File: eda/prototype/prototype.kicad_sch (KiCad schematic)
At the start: 45 parts, among them J1 Conn_02x05_Odd_Even, SW1 SW_DIP_x04, U1 8088_Min_Mode, U10 8255A, U11 8253, U12 8259A, U13 8251, U2 GAL16V8, U3 74HC161, U4 74HC574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

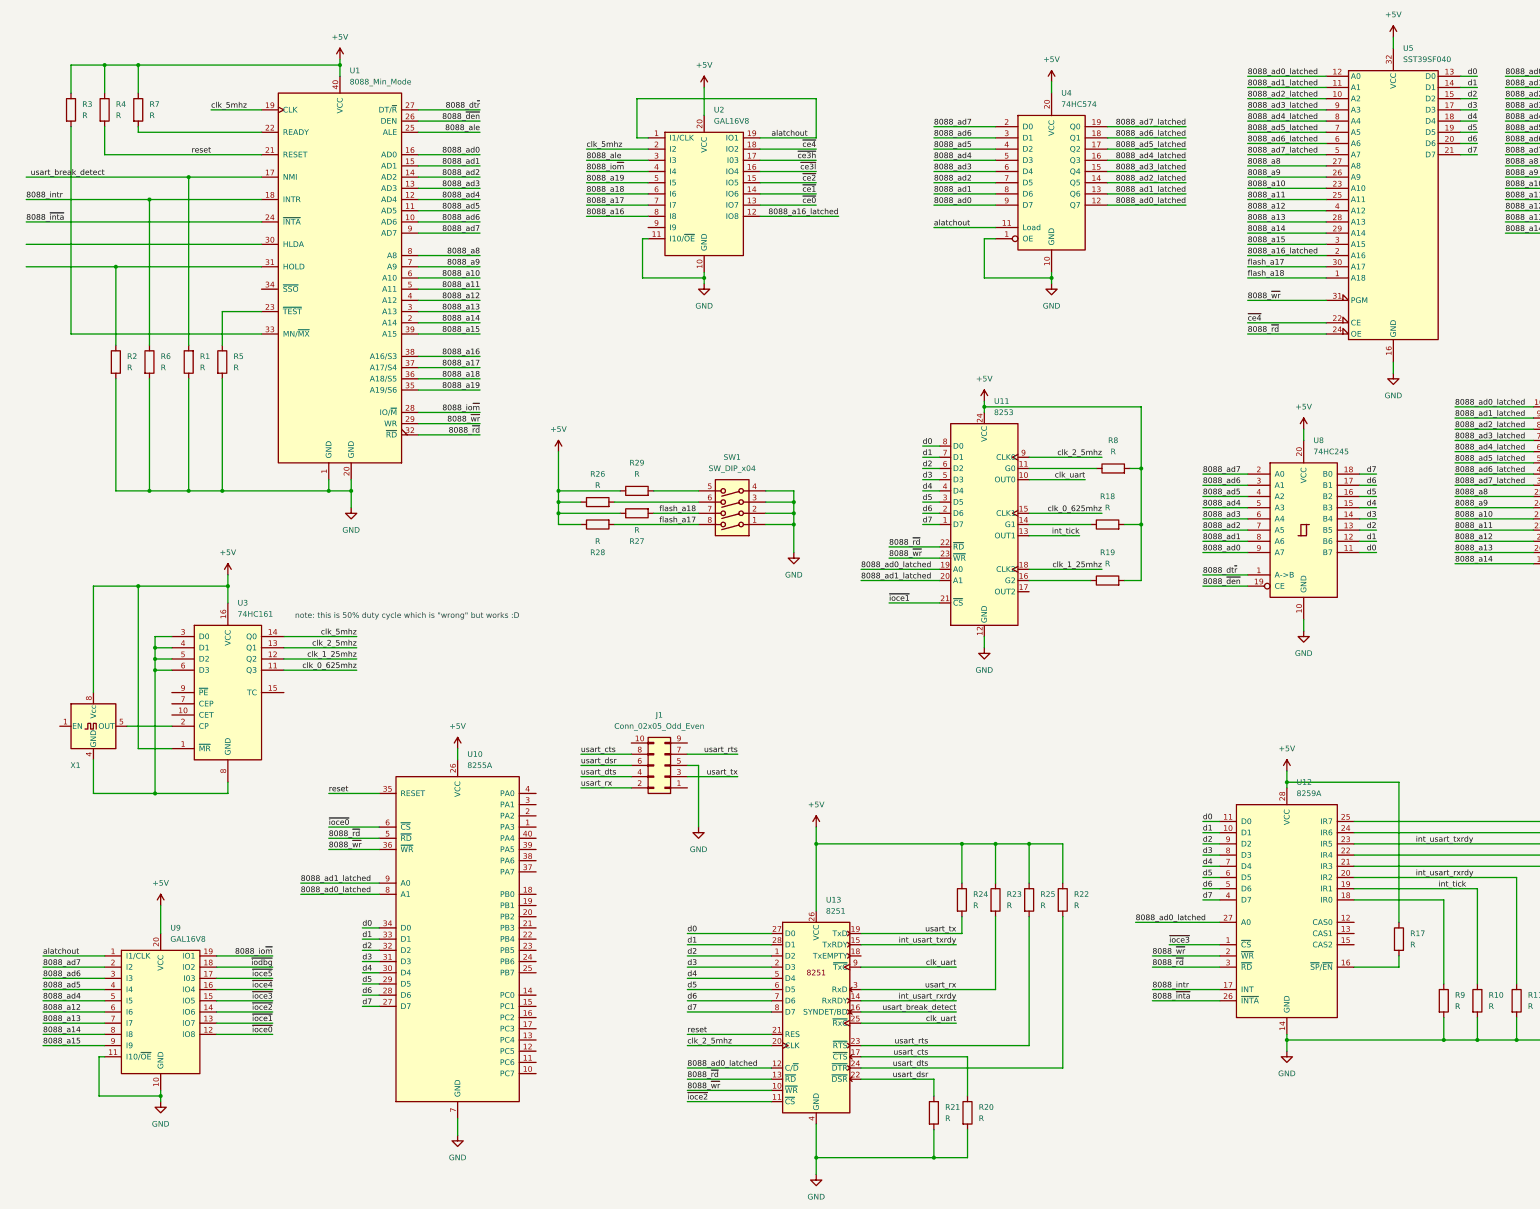
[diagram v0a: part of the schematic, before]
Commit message: eda: prototype: sync schematic
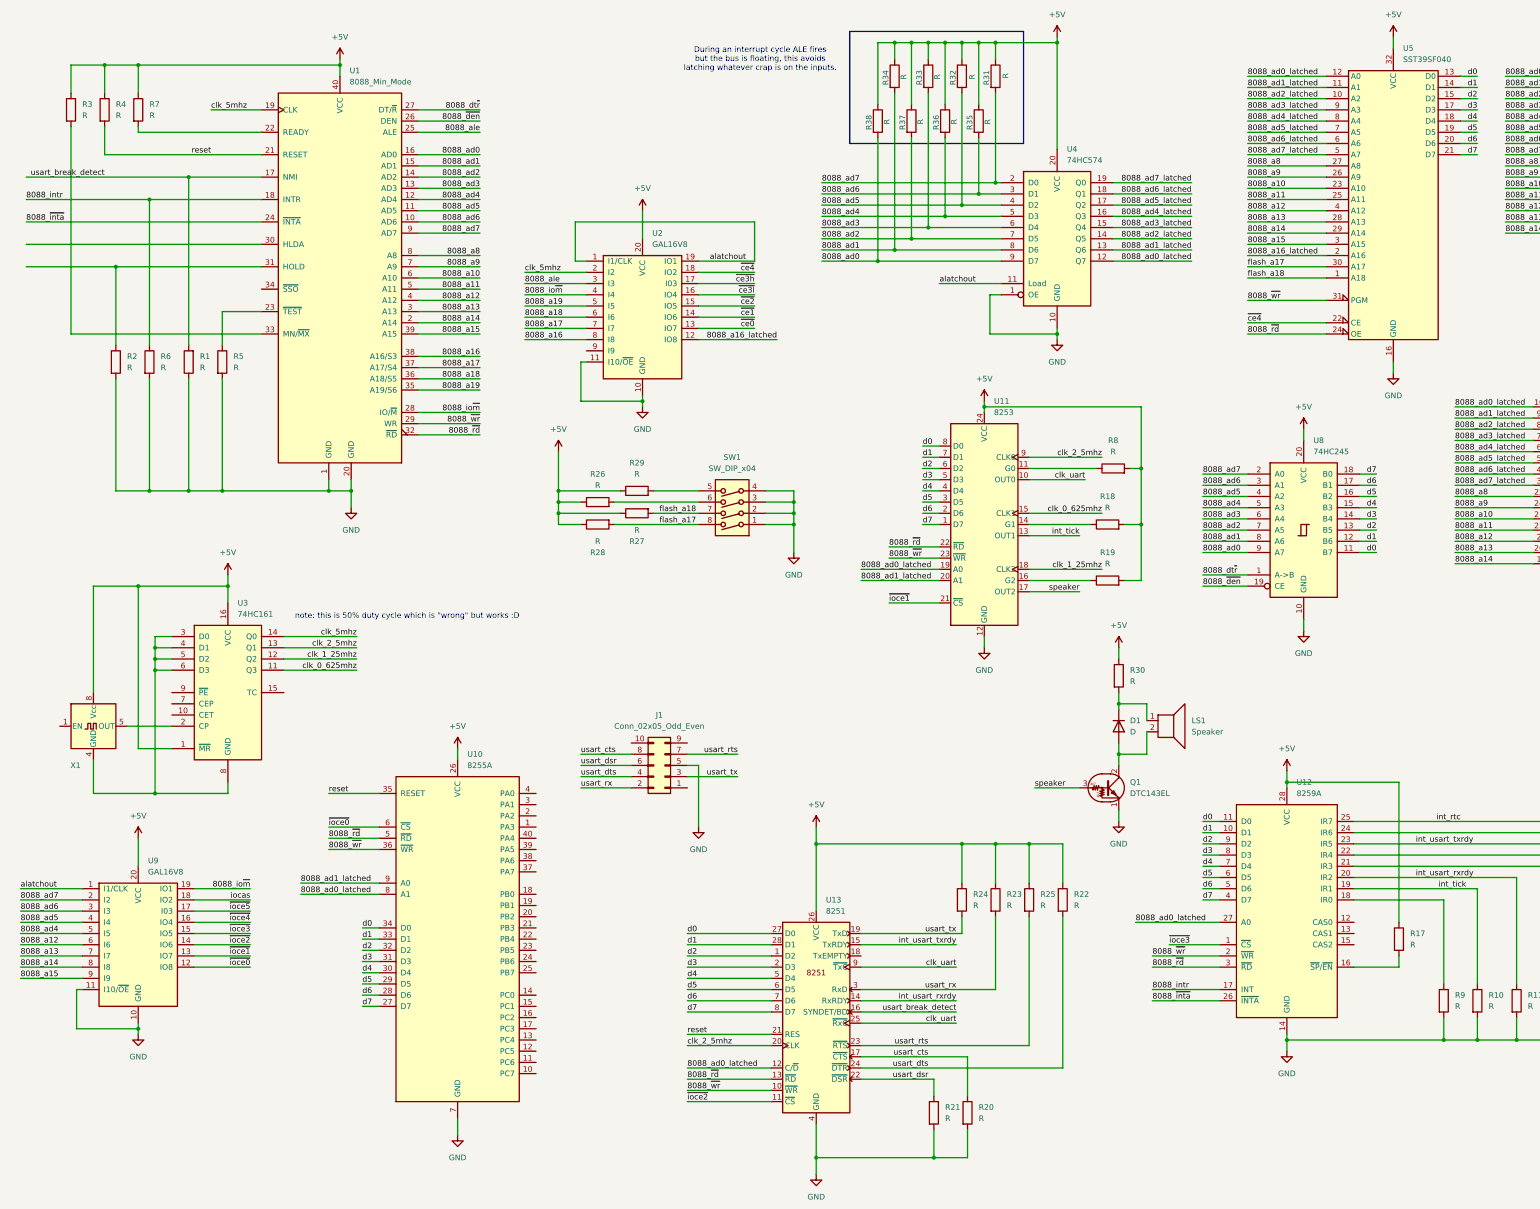
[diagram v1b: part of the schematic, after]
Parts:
- added D1: D, symbol Device:D
- added LS1: Speaker, symbol Device:Speaker
- added Q1: DTC143EL, symbol Transistor_BJT:DTC143E
- added R30, R31, R32, R33, R34, R35, R36, R37, R38: R, symbol Device:R
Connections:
- net +5V: now also R30.1, R31.1, R32.1, R33.1, R34.1, R35.1, R36.1, R37.1, R38.1
- net 8088_ad0: now also R38.2
- net 8088_ad1: now also R34.2
- net 8088_ad2: now also R37.2
- net 8088_ad3: now also R33.2
- net 8088_ad4: now also R36.2
- net 8088_ad5: now also R32.2
- net 8088_ad6: now also R35.2
- net 8088_ad7: now also R31.2
- net GND: now also Q1.1 (E)
- net int_rtc: now reaches R16.1, U12.25 (IR7)
- net speaker: now reaches U11.17 (OUT2)
- net speaker: now also Q1.3 (B)
- net ~{iodbg} renamed iocas
- new net: D1.1 (K), LS1.1, R30.2
- new net: D1.2 (A), LS1.2, Q1.2 (C)
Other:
- note added: "During an interrupt cycle ALE fires but the bus is floating, this avoids latching whatever crap is on the inputs."
- moved on the sheet: U2, U4, U9

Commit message: eda:prototype: jankorama rng
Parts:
- removed U2, U9: GAL16V8, symbol Logic_Programmable:GAL16V8
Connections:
- net clk_10mhz: now reaches U3.2 (CP), X1.5 (OUT)
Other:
- added sheet PLDs (plds.kicad_sch)
- added sheet RNG (rng.kicad_sch)

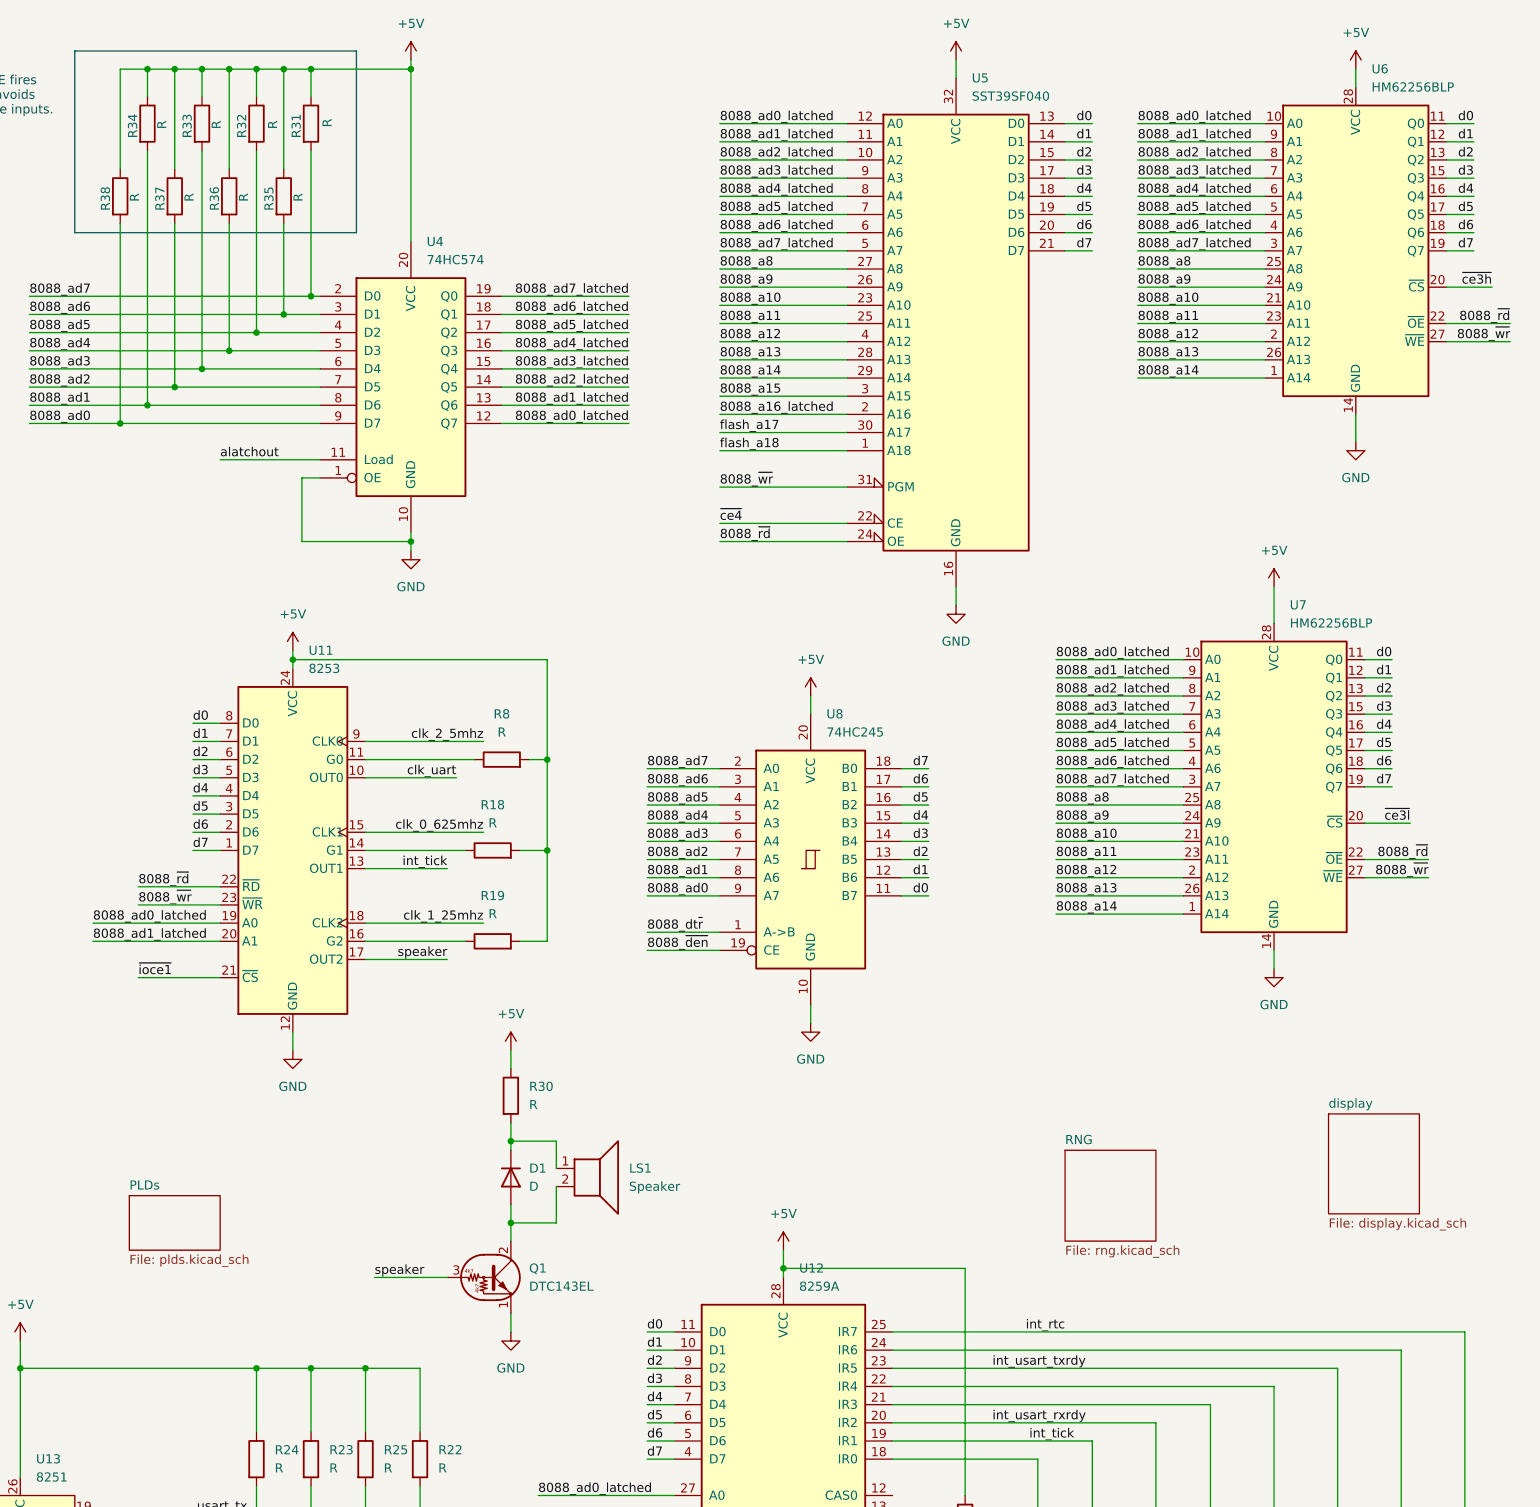
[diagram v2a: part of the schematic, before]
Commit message: eda: prototype: Split up a bit, add RTC
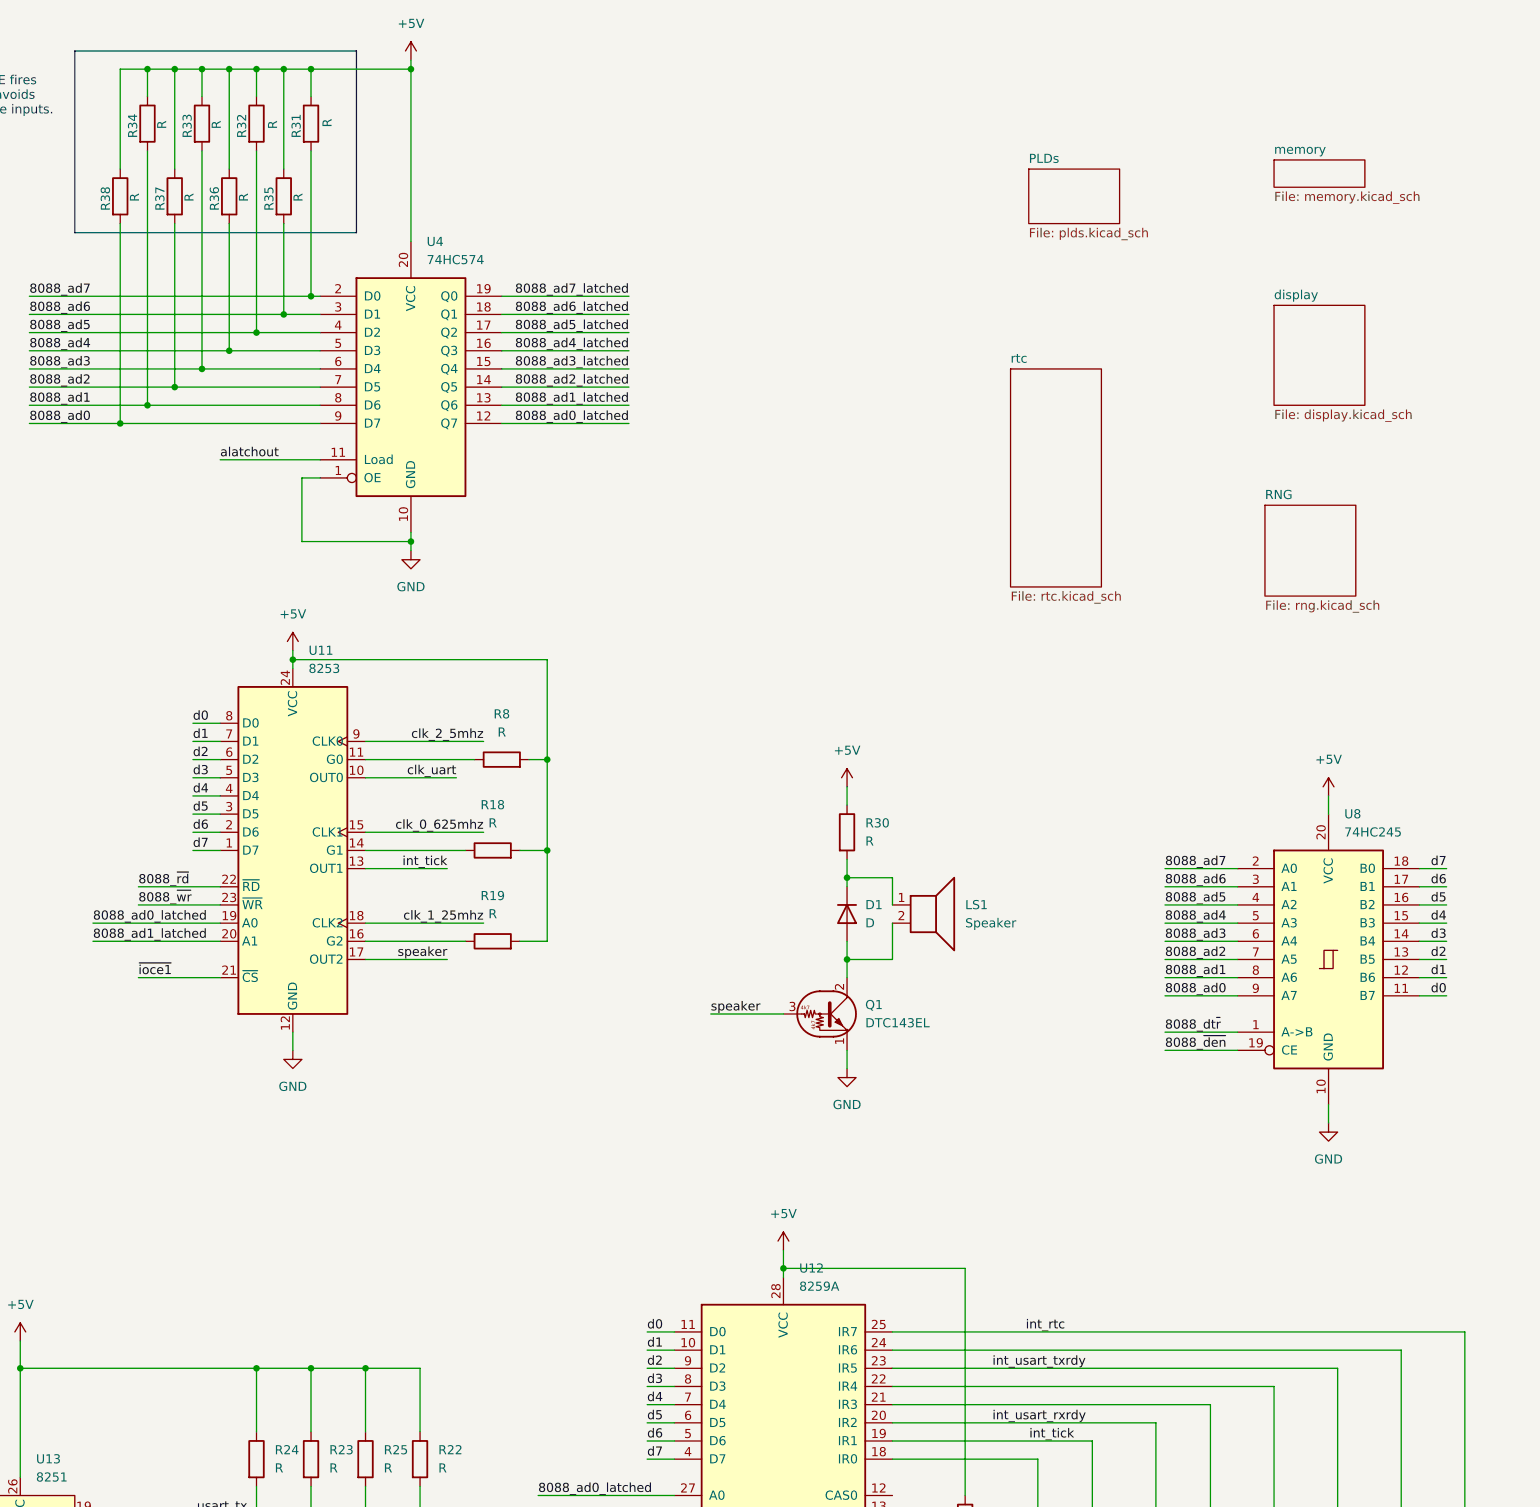
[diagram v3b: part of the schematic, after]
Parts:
- removed U5: SST39SF040, symbol Memory_Flash:SST39SF040
- removed U6, U7: HM62256BLP, Package_DIP:DIP-28_W15.24mm, symbol Memory_RAM:HM62256BLP
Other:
- added sheet memory (memory.kicad_sch)
- added sheet rtc (rtc.kicad_sch)
- moved on the sheet: D1, LS1, Q1, R30, U8
